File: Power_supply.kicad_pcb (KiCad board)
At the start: 2 copper layers, 190 x 110 mm, 26 parts, among them J1 AudioJack3, J10 output, J11 Conn_01x03, J12 Conn_01x03, J13 Conn_01x04, J3 Conn_01x04, J5 220V, J7 Conn_01x04, J9 output, SW1 SW_Push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

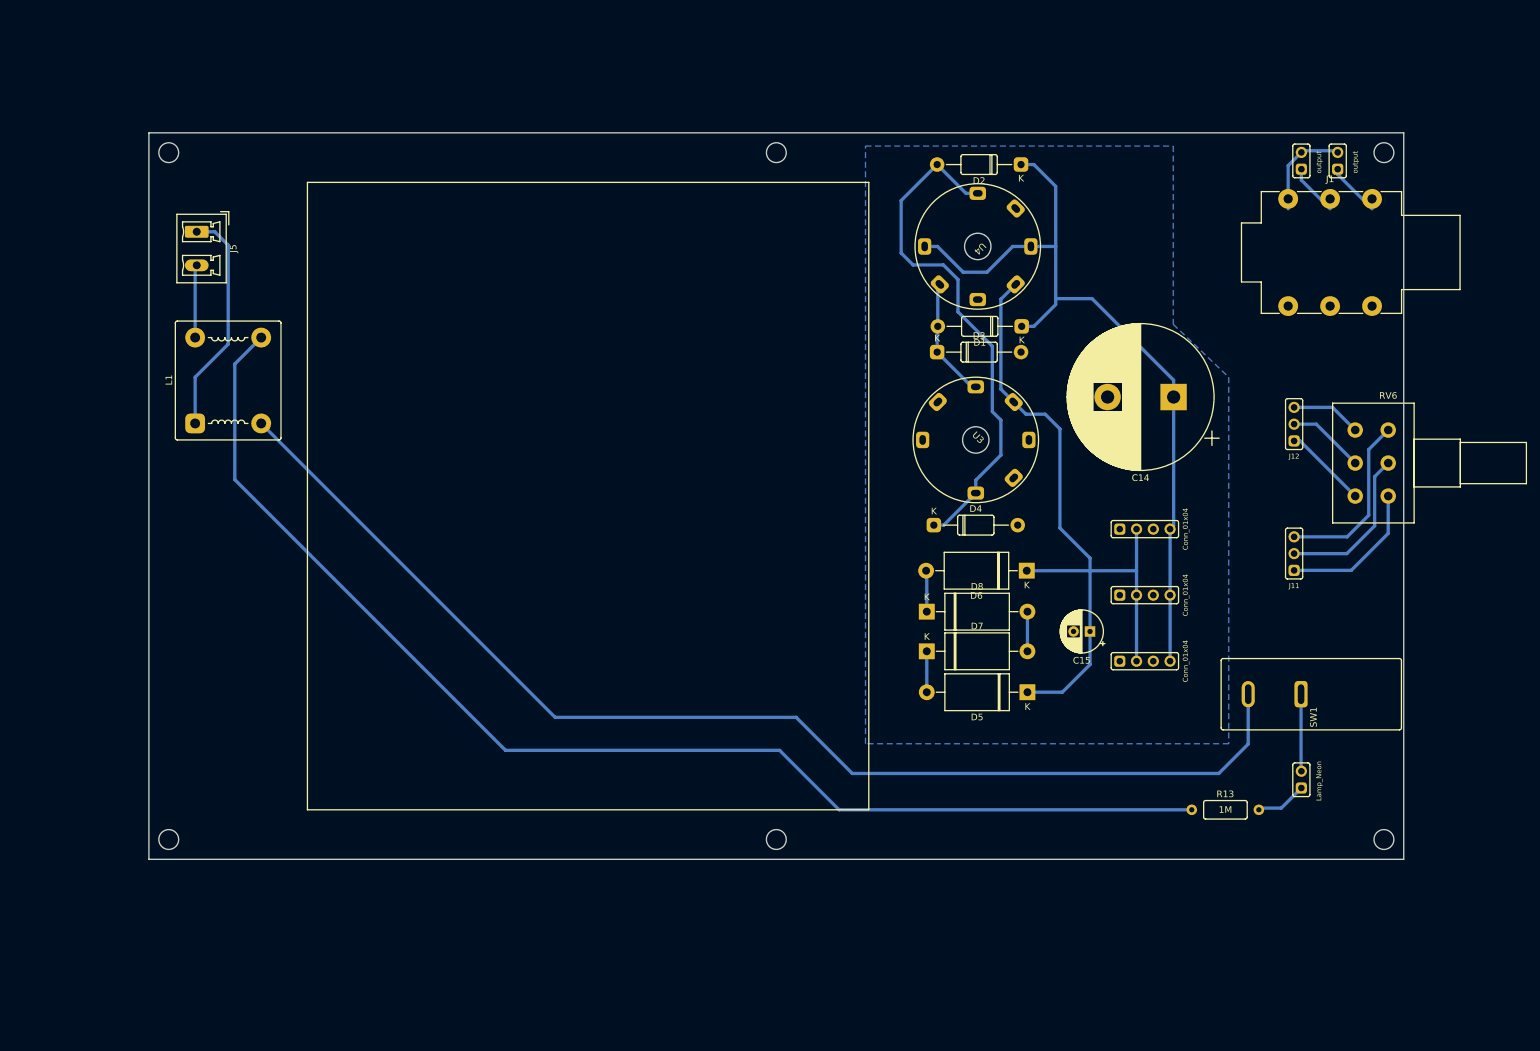
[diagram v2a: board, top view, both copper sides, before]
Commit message: High Voltage stabilizer
Create high voltage stabilizer
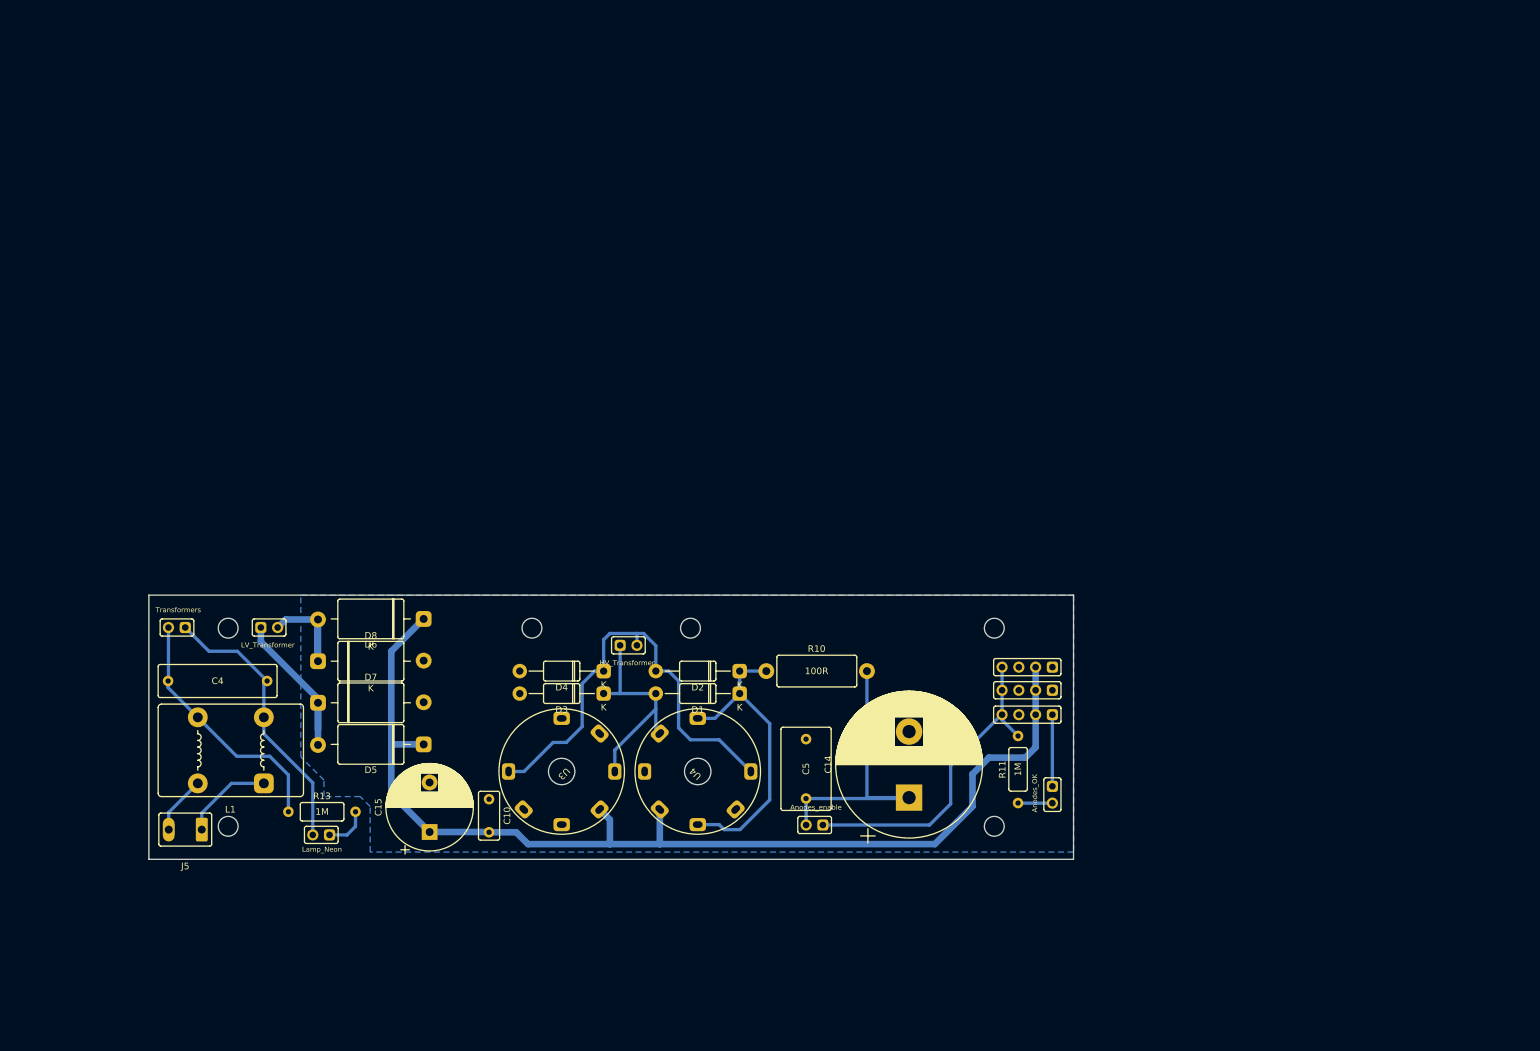
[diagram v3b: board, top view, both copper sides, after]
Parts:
- removed J1: AudioJack3, Connector_Audio:Jack_6.35mm_Neutrik_NMJ6HHD2_Horizontal
- removed J10, J9: output, spdf1626_lib:PinHeader_1x02_P2.54mm
- removed J11, J12: Conn_01x03, spdf1626_lib:PinHeader_1x03_P2.54mm
- removed RV6: R_Potentiometer_Dual, Potentiometer_THT:Potentiometer_Alps_RK163_Dual_Horizontal
- removed SW1: SW_Push, Button_Switch_THT:SW_Push_1P2T_Vertical_E-Switch_800UDP8P1A1M6
- added C10: 100n, spdf1626_lib:C_THT_K73-17_P5.00mm, F.Cu at (101.5, 120.9)
- added C4: 100n, spdf1626_lib:C_THT_K73-17_P15.00mm, F.Cu at (60.4, 103.0)
- added C5: 100n, spdf1626_lib:C_THT_K73-17_P9.00mm, F.Cu at (149.5, 116.3)
- added J14: HV_Transformer, spdf1626_lib:PinHeader_1x02_P2.54mm, F.Cu at (121.3, 97.6)
- added J15: LV_Transformer, spdf1626_lib:PinHeader_1x02_P2.54mm, F.Cu at (67.0, 94.9)
- added J16: Transformers, spdf1626_lib:PinHeader_1x02_P2.54mm, F.Cu at (55.5, 94.9)
- added J18: Anodes_enable, spdf1626_lib:PinHeader_1x02_P2.54mm, F.Cu at (152.0, 124.8)
- added NE2: Anodes_OK, spdf1626_lib:PinHeader_1x02_P2.54mm, F.Cu at (186.8, 119.0)
- added R10: 100R, spdf1626_lib:R_THT_1W, F.Cu at (143.5, 101.5)
- added R11: 1M, spdf1626_lib:R_THT_025W, F.Cu at (181.6, 121.5)
- C15: value 100uF_10V -> 3300uF_10V; footprint Capacitor_THT:CP_Radial_D6.3mm_P2.50mm -> Capacitor_THT:CP_Radial_D13.0mm_P7.50mm
- D5, D6, D7, D8: value 10A10 -> 1N5821; footprint Diode_THT:D_DO-27_P15.24mm_Horizontal -> spdf1626_lib:D_DO-27_P16mm_Horizontal
- J5: footprint Connector_Phoenix_MC_HighVoltage:PhoenixContact_MCV_1,5_2-G-5.08_1x02_P5.08mm_Vertical -> spdf1626_lib:Connector_1x02_P5mm_Vertical
- L1: footprint spdf1626_lib:L_THT_PLA10 -> spdf1626_lib:L_THT_B82731-T
- moved NE1 147.3 mm to (77.3, 126.3), turned to -90 degrees
- moved R13 136.8 mm to (71.1, 122.8)
- moved C15 104.5 mm to (92.5, 125.9), turned to 90 degrees
- moved D5 99.7 mm to (83.6, 112.6)
- moved D6 99.6 mm to (83.6, 93.6)
- moved J5 90.5 mm to (55.5, 125.5), turned to 180 degrees
- moved U4 90.1 mm to (133.1, 116.7), turned to 135 degrees
- moved D2 87.7 mm to (139.4, 101.5)
- moved D7 84.5 mm to (83.6, 106.3)
- moved D8 84.5 mm to (83.6, 100.0)
- moved U3 80.3 mm to (112.5, 116.7), turned to -135 degrees
- moved C14 72.7 mm to (165.1, 120.7), turned to 90 degrees
- moved D3 72.3 mm to (118.8, 104.9), turned to 180 degrees
- moved D1 70.1 mm to (139.4, 104.9)
- moved L1 56.0 mm to (62.4, 113.5), turned to 180 degrees
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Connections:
- C14 pad 1: 240V -> Net-(C14-Pad1)
- D1 pad 1: 240V -> 240V_rect
- D2 pad 1: 240V -> 240V_rect
- L1 pad 2: Net-(L1-Pad2) -> Net-(NE1-Pad2)
- U4 pad 1: 240V -> 240V_rect
- U4 pad 5: 240V -> 240V_rect
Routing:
- net Net-(L1-Pad2): track 181.8 -> 0.00 mm
- net Net-(L1-Pad3): track 188.8 -> 38.4 mm
- net 240V: track 120.1 -> 48.9 mm
- net +6V: track 113.6 -> 166.4 mm
- net 240V_rect: track 0.00 -> 46.4 mm
- net Net-(C14-Pad1): track 0.00 -> 45.2 mm
- net Net-(NE1-Pad2): track 12.7 -> 42.3 mm
- net Net-(J11-Pad3): track 26.8 -> 0.00 mm
- net Net-(J11-Pad2): track 24.3 -> 0.00 mm
- net Net-(J11-Pad1): track 22.2 -> 0.00 mm
- net Net-(D5-Pad2): track 6.20 -> 27.8 mm
- net Net-(J5-Pad1): track 34.7 -> 13.8 mm
- net 240_2: track 18.4 -> 33.5 mm
- net Net-(D6-Pad2): track 6.24 -> 19.3 mm
- net Net-(J12-Pad1): track 12.7 -> 0.00 mm
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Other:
- board size 190 x 110 mm -> 140 x 40 mm

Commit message: Multiple PCB
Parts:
- removed C10: 100n, spdf1626_lib:C_THT_K73-17_P5.00mm
- removed C14: 100uF, Capacitor_THT:CP_Radial_D22.0mm_P10.00mm_SnapIn
- removed C15: 3300uF_10V, Capacitor_THT:CP_Radial_D13.0mm_P7.50mm
- removed C4: 100n, spdf1626_lib:C_THT_K73-17_P15.00mm
- removed C5: 100n, spdf1626_lib:C_THT_K73-17_P9.00mm
- removed D1, D2, D3, D4: 1n4007, spdf1626_lib:D_DO-41
- removed D5, D6, D7, D8: 1N5821, spdf1626_lib:D_DO-27_P16mm_Horizontal
- removed J13, J3, J7: Conn_01x04, spdf1626_lib:PinHeader_1x04_P2.54mm
- removed J14: HV_Transformer, spdf1626_lib:PinHeader_1x02_P2.54mm
- removed J15: LV_Transformer, spdf1626_lib:PinHeader_1x02_P2.54mm
- removed J16: Transformers, spdf1626_lib:PinHeader_1x02_P2.54mm
- removed J18: Anodes_enable, spdf1626_lib:PinHeader_1x02_P2.54mm
- removed J5: 220V, spdf1626_lib:Connector_1x02_P5mm_Vertical
- removed L1: L_Coupled, spdf1626_lib:L_THT_B82731-T
- removed NE1: Lamp_Neon, spdf1626_lib:PinHeader_1x02_P2.54mm
- removed NE2: Anodes_OK, spdf1626_lib:PinHeader_1x02_P2.54mm
- removed R10: 100R, spdf1626_lib:R_THT_1W
- removed R11, R13: 1M, spdf1626_lib:R_THT_025W
- removed U3: 6H2P, spdf1626_lib:7-pin_tube_socket
- added C24: 100n, spdf1626_lib:C_THT_K73-17_P15.00mm, F.Cu at (64.0, 102.0)
- added C25: 3300uF_10V, Capacitor_THT:CP_Radial_D13.0mm_P7.50mm, F.Cu at (117.0, 114.1)
- added C26: 100n, spdf1626_lib:C_THT_K73-17_P9.00mm, F.Cu at (113.9, 45.6)
- added C27: 100n, spdf1626_lib:C_THT_K73-17_P9.00mm, F.Cu at (105.5, 110.5)
- added C28: 10uF, spdf1626_lib:C_THT_D10.0mm_P5.00mm, F.Cu at (94.6, 28.1)
- added C29: 100n, spdf1626_lib:C_THT_K73-17_P9.00mm, F.Cu at (139.9, 12.1)
- added C30: 100n, spdf1626_lib:C_THT_K73-17_P9.00mm, F.Cu at (95.3, 56.7)
- added C31: 10uF, spdf1626_lib:C_THT_D10.0mm_P5.00mm, F.Cu at (165.8, 9.17)
- added C32: 10uF, spdf1626_lib:C_THT_D10.0mm_P5.00mm, F.Cu at (145.0, 31.5)
- added C33: 100uF, Capacitor_THT:CP_Radial_D22.0mm_P10.00mm_SnapIn, F.Cu at (166.0, 117.0)
- added D12: 1n4007, spdf1626_lib:D_DO-41, F.Cu at (138.3, 108.6)
- added D13: 1n4007, spdf1626_lib:D_DO-41, F.Cu at (138.3, 112.0)
- added D14: 1n4007, spdf1626_lib:D_DO-41, F.Cu at (125.7, 105.2)
- added D15: 1n4007, spdf1626_lib:D_DO-41, F.Cu at (125.7, 101.8)
- added D16: 1N5821, spdf1626_lib:D_DO-27_P16mm_Horizontal, F.Cu at (92.0, 121.5)
- added D17: 1N5821, spdf1626_lib:D_DO-27_P16mm_Horizontal, F.Cu at (92.0, 115.0)
- added D18: 1N5821, spdf1626_lib:D_DO-27_P16mm_Horizontal, F.Cu at (92.0, 102.0)
- added D19: 1N5821, spdf1626_lib:D_DO-27_P16mm_Horizontal, F.Cu at (92.0, 108.5)
- added D20: 1n4007, spdf1626_lib:D_DO-41, F.Cu at (210.8, 42.4)
- added J20: HV_Transformer, spdf1626_lib:PinHeader_1x02_P2.54mm, F.Cu at (118.8, 95.0)
- added J21: LV_Transformer, spdf1626_lib:PinHeader_1x02_P2.54mm, F.Cu at (84.0, 95.0)
- added J22: 220V, spdf1626_lib:Connector_1x02_P5mm_Vertical, F.Cu at (71.0, 125.0)
- added J23: Transformers, spdf1626_lib:PinHeader_1x02_P2.54mm, F.Cu at (72.0, 95.0)
- added J24: Thyratrone, spdf1626_lib:PinHeader_1x03_P2.54mm, F.Cu at (120.5, 56.7)
- added J25: Anodes_enable, spdf1626_lib:PinHeader_1x02_P2.54mm, F.Cu at (151.6, 155.7)
- added J26: Conn_01x04, spdf1626_lib:PinHeader_1x04_P2.54mm, F.Cu at (186.8, 115.0)
- added J27: Conn_01x04, spdf1626_lib:PinHeader_1x04_P2.54mm, F.Cu at (186.8, 110.0)
- added J28: Conn_01x04, spdf1626_lib:PinHeader_1x04_P2.54mm, F.Cu at (186.8, 105.0)
- added K2: SANYOU_SRD_Form_C, Relay_THT:Relay_SPDT_SANYOU_SRD_Series_Form_C, F.Cu at (216.5, 48.7)
- added L2: L_Coupled, spdf1626_lib:L_THT_B82731-T, F.Cu at (64.0, 113.0)
- added NE3: Lamp_Neon, spdf1626_lib:PinHeader_1x02_P2.54mm, F.Cu at (78.0, 125.0)
- added NE4: Anodes_OK, spdf1626_lib:PinHeader_1x02_P2.54mm, F.Cu at (175.9, 13.2)
- added Q10: MPSA42, Package_TO_SOT_THT:TO-92_Inline, F.Cu at (134.5, 53.2)
- added Q11: MJE13003, Package_TO_SOT_THT:TO-126-3_Vertical, F.Cu at (155.9, 18.4)
- added Q12: 2N3904, Package_TO_SOT_THT:TO-92_Inline, F.Cu at (165.2, 18.1)
- added Q7: MPSA42, Package_TO_SOT_THT:TO-92_Inline, F.Cu at (139.3, 43.4)
- added Q8: MPSA42, Package_TO_SOT_THT:TO-92_Inline, F.Cu at (124.3, 63.9)
- added Q9: MPSA42, Package_TO_SOT_THT:TO-92_Inline, F.Cu at (124.3, 58.1)
- added R26: 100R, spdf1626_lib:R_THT_1W, F.Cu at (90.1, 45.1)
- added R27: 1M, spdf1626_lib:R_THT_025W, F.Cu at (78.0, 107.9)
- added R28: 13k, spdf1626_lib:R_THT_025W, F.Cu at (148.1, 13.6)
- added R29: 10k, spdf1626_lib:R_THT_025W, F.Cu at (122.1, 41.5)
- added R30: 600R, spdf1626_lib:R_THT_025W, F.Cu at (125.8, 36.7)
- added R31: 100k, spdf1626_lib:R_THT_025W, F.Cu at (98.8, 63.0)
- added R32: 100k, spdf1626_lib:R_THT_025W, F.Cu at (86.1, 64.2)
- added R33: 1M, spdf1626_lib:R_THT_025W, F.Cu at (103.5, 58.2)
- added R34: 50k, spdf1626_lib:R_THT_025W, F.Cu at (125.8, 32.8)
- added R35: 40k, spdf1626_lib:R_THT_025W, F.Cu at (148.1, 9.70)
- added R36: 1M, spdf1626_lib:R_THT_025W, F.Cu at (103.5, 54.3)
- added RV3: 10k, spdf1626_lib:Potentiometer_THT_CA9V, F.Cu at (129.8, 25.8)
- U4: value 6H2P -> SG2P
- moved U4 84.6 mm to (78.4, 52.2), turned to 0 degrees
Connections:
- U4 pad 1: 240V_rect -> Net-(C28-Pad2)
- U4 pad 2: 240_2 -> unconnected-(U4-Pad2)
- U4 pad 3: GND -> (no net)
- U4 pad 4: +6V -> GND
- U4 pad 5: 240V_rect -> unconnected-(U4-Pad5)
- U4 pad 6: GND -> (no net)
- U4 pad 7: 240_1 -> unconnected-(U4-Pad7)
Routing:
- net +6V: track 166.4 -> 0.00 mm
- net 240_1: track 68.8 -> 0.00 mm
- net 240V: track 48.9 -> 0.00 mm
- net 240V_rect: track 46.4 -> 0.00 mm
- net Net-(C14-Pad1): track 45.2 -> 0.00 mm
- net Net-(NE1-Pad2): track 42.3 -> 0.00 mm
- net Net-(L1-Pad3): track 38.4 -> 0.00 mm
- net 240_2: track 33.5 -> 0.00 mm
- net Net-(D5-Pad2): track 27.8 -> 0.00 mm
- net Net-(D6-Pad2): track 19.3 -> 0.00 mm
- net Net-(J5-Pad1): track 13.8 -> 0.00 mm
- net GND: track 10.9 -> 0.00 mm
- net Net-(J5-Pad2): track 8.82 -> 0.00 mm
- net Net-(NE1-Pad1): track 6.68 -> 0.00 mm
- net Net-(NE2-Pad2): track 5.20 -> 0.00 mm
- removed copper zone on B.Cu, net GND
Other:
- outline, holes or cut-outs redrawn
